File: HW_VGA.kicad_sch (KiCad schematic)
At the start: 6 parts, among them U1 74HC163, U2 74HC163, U3 74HC163, U4 25.175 MHz, U5 74HC11, U6 74HC688

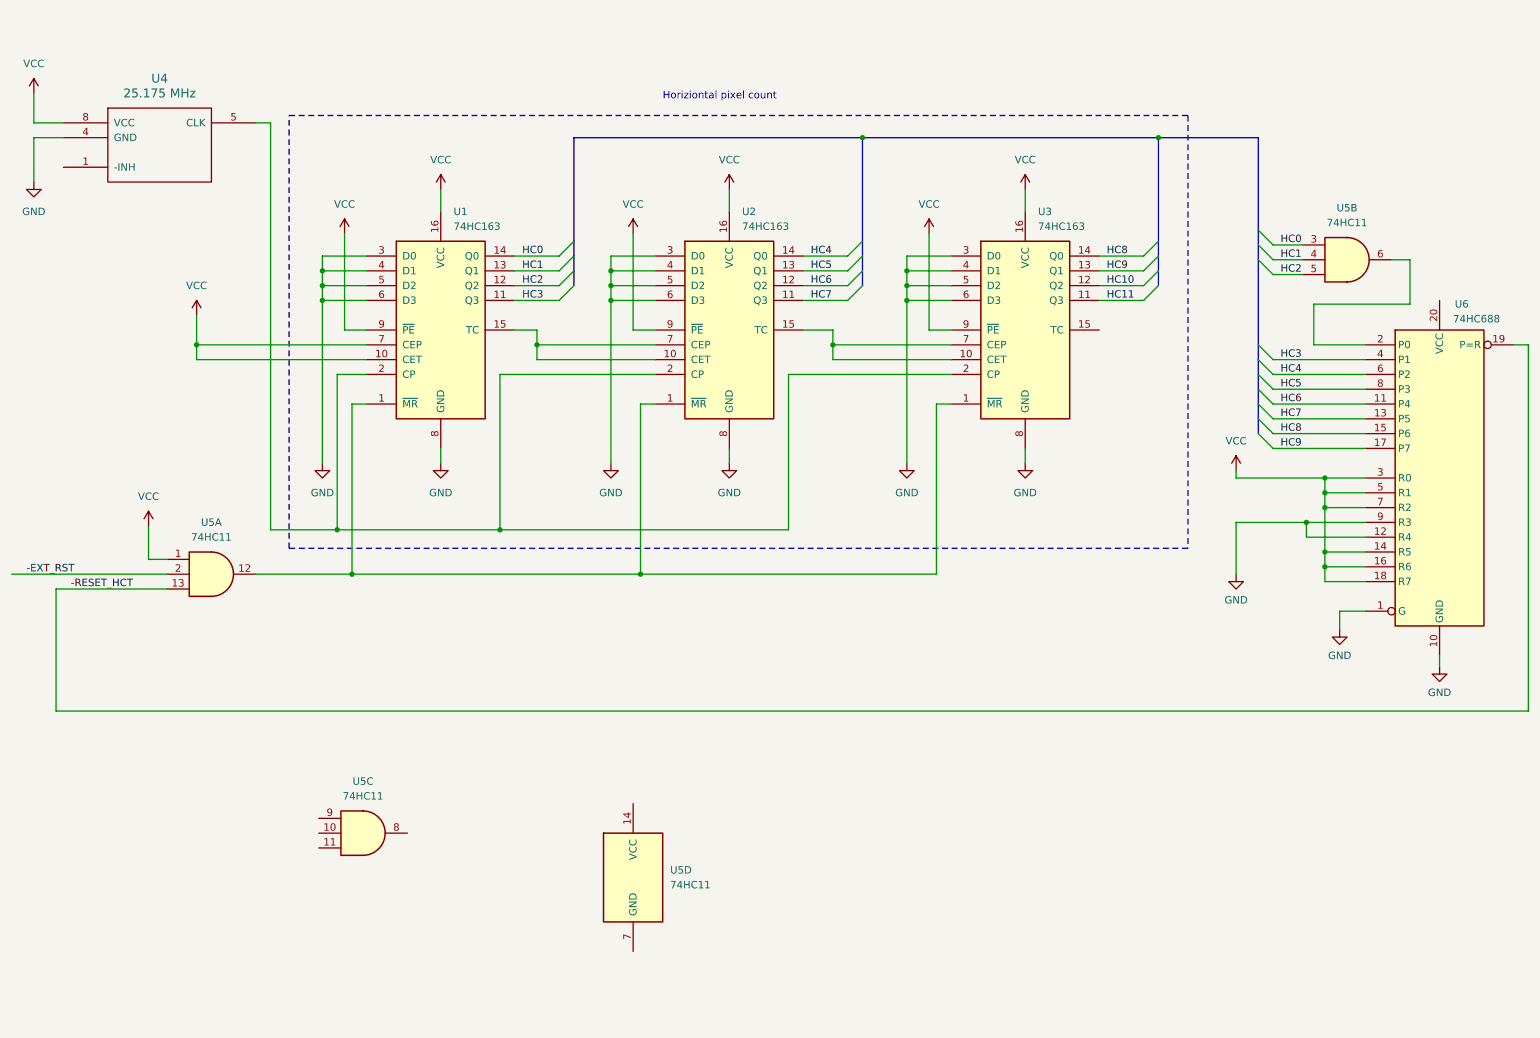
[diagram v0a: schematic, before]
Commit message: move horizontal count module to separate sheet
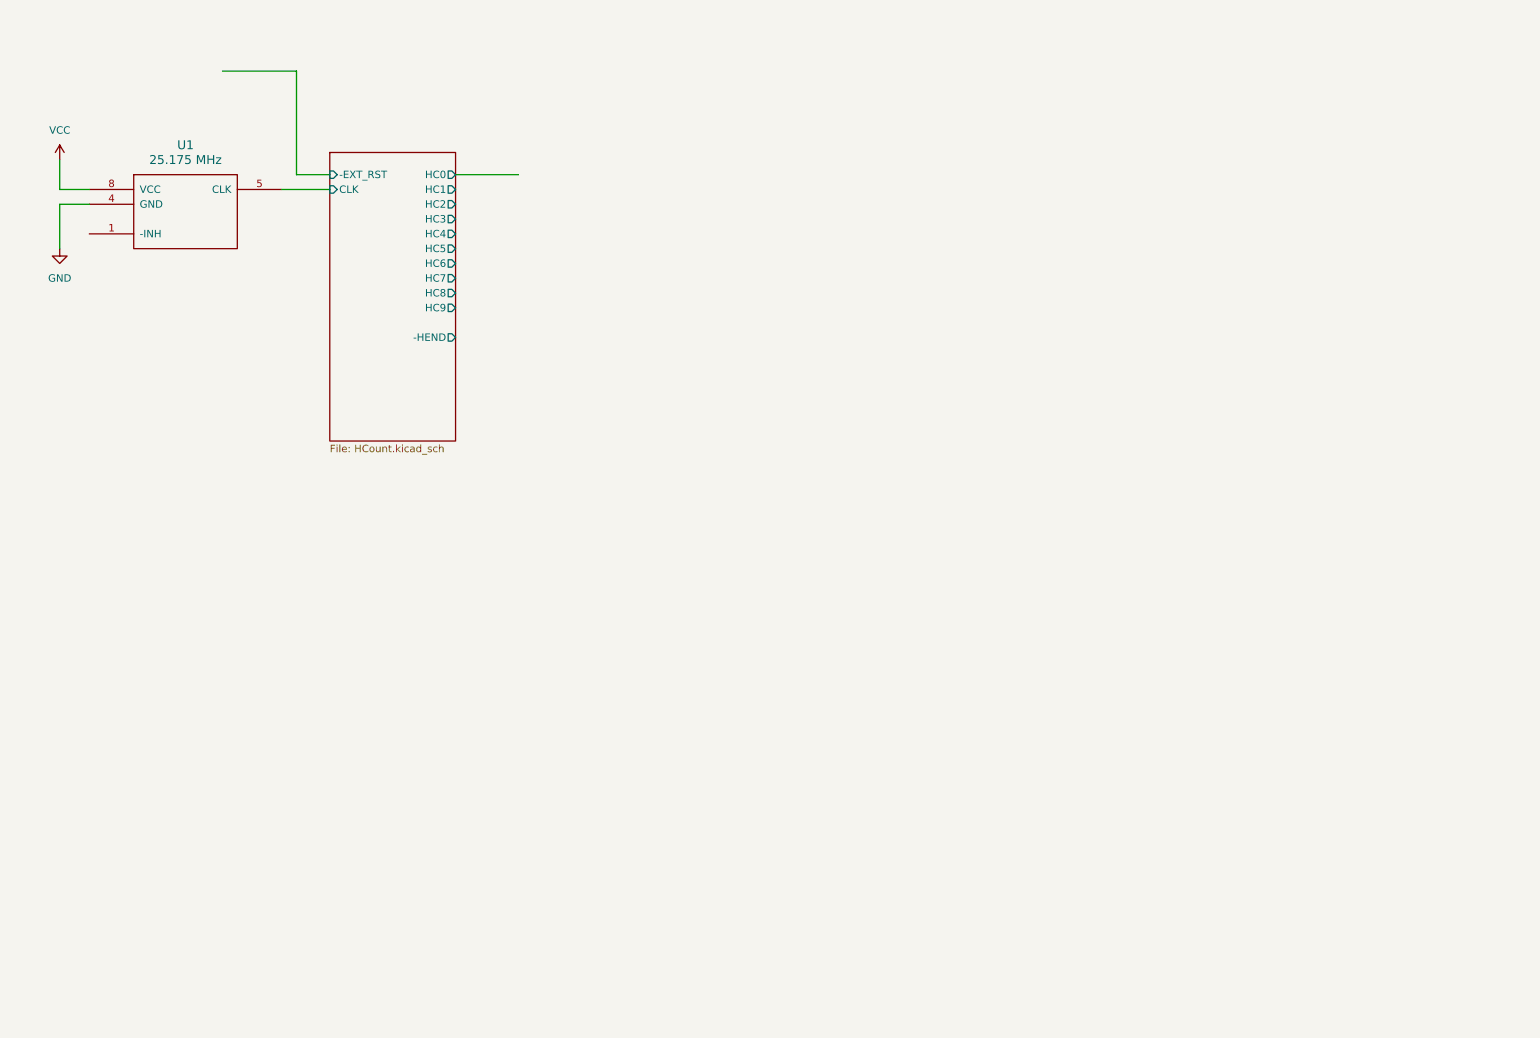
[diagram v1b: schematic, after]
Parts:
- removed U1, U2, U3: 74HC163, symbol 74xx:74LS163
- removed U4: 25.175 MHz, symbol ya68k:XTAL_OSC_HALF_CAN
- removed U5: 74HC11, symbol 74xx:74LS11
- removed U6: 74HC688, symbol 74xx:74LS688
- added U1: 25.175 MHz, symbol ya68k:XTAL_OSC_HALF_CAN
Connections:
- net GND: now also U1.4 (GND)
- net VCC: now also U1.8 (VCC)
- new net HCount/CLK: U1.5 (CLK)
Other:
- added sheet HCount (HCount.kicad_sch)
- note removed: "Horiziontal pixel count"
- company: (none) -> daveho hacks
- title: (none) -> Hardware VGA

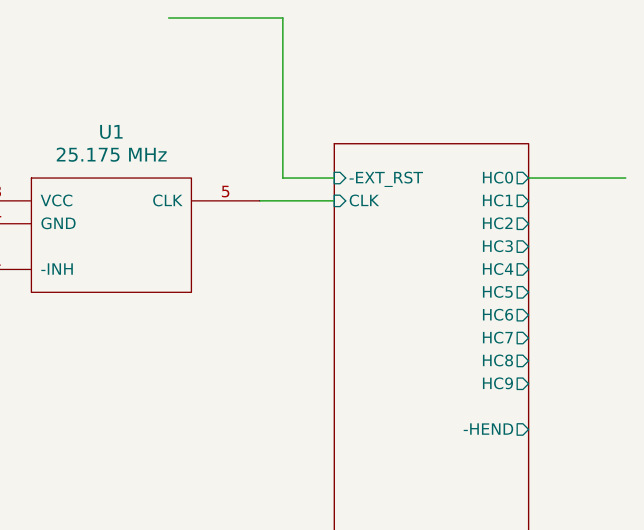
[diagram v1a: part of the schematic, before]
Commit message: allow hcount reset when frame ends
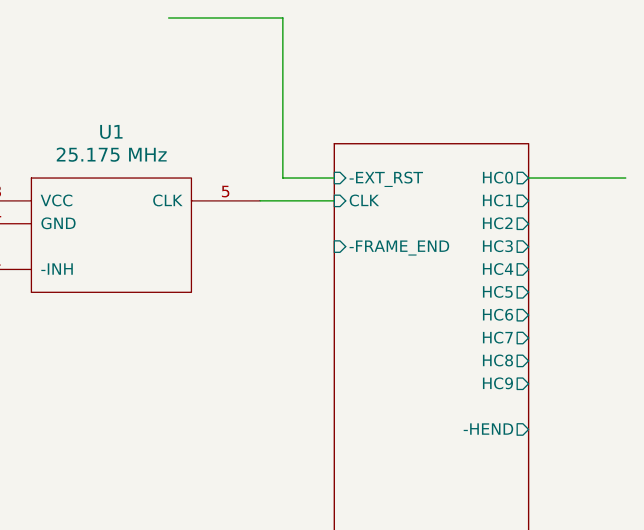
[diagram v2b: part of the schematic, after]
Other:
- sheet HCount ports: added -FRAME_END; removed none
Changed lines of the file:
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@@
       (effects (font (size 1.27 1.27)) (justify right))
+    )
+    (pin "-FRAME_END" input (at 73.66 50.8 180)
+      (effects (font (size 1.27 1.27)) (justify left))
     )
     (instances

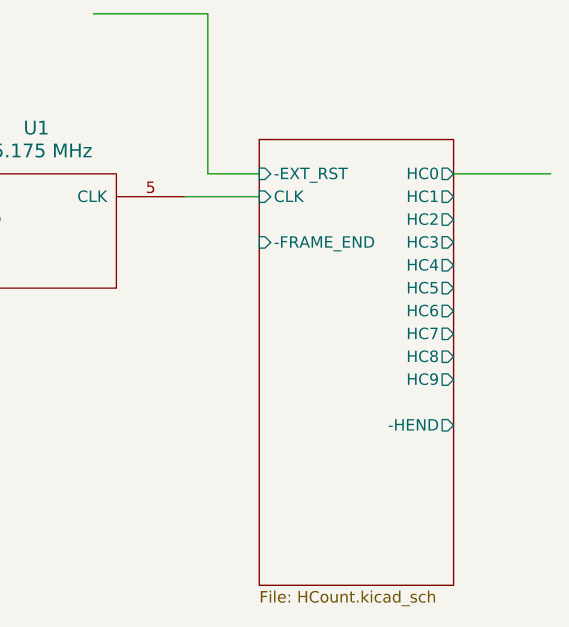
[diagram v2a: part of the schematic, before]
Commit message: replace horizontal count logic with GAL22V10
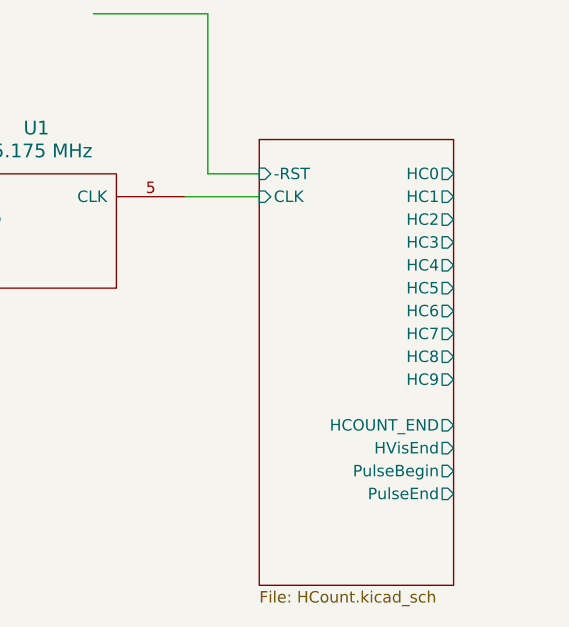
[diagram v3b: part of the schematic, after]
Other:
- sheet HCount ports: added -RST, HCOUNT_END, HVisEnd, PulseBegin, PulseEnd; removed -EXT_RST, -FRAME_END, -HEND

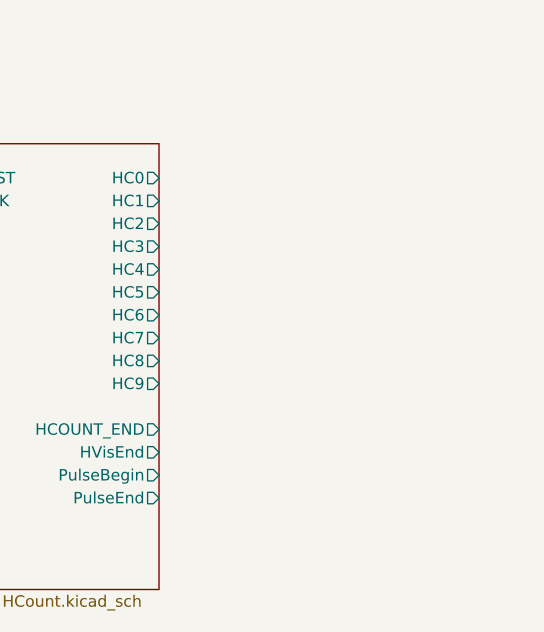
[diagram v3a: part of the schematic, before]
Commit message: start working on VCount module
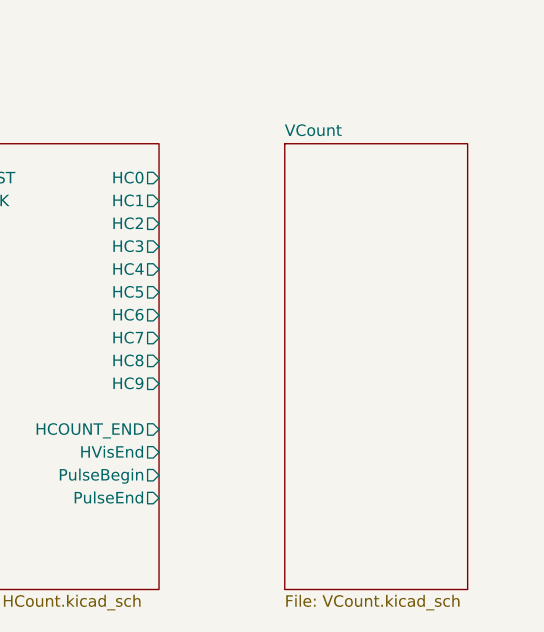
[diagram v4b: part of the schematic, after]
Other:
- added sheet VCount (VCount.kicad_sch)
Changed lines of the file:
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@@
+		)
+	)
+	(sheet
+		(at 109.22 39.37)
+		(size 20.32 49.53)
+		(fields_autoplaced yes)
+		(stroke
+			(width 0.1524)
+			(type solid)
+		)
+		(fill
+			(color 0 0 0 0.0000)
+		)
+		(property "Sheetname" "VCount"
+			(at 109.22 38.6584 0)
+			(effects
+				(font
+					(size 1.27 1.27)
+				)
+				(justify left bottom)
+			)
+		)
+		(property "Sheetfile" "VCount.kicad_sch"
+			(at 109.22 89.4846 0)
+			(effects
+				(font
+					(size 1.27 1.27)
+				)
+				(justify left top)
+			)
+		)
+		(instances
+			(project "HW_VGA"
+				(path "/c4bd4b39-993a-4195-805f-b4de6fa4aea5"
+					(page "3")
+				)
+			)
 		)
 	)

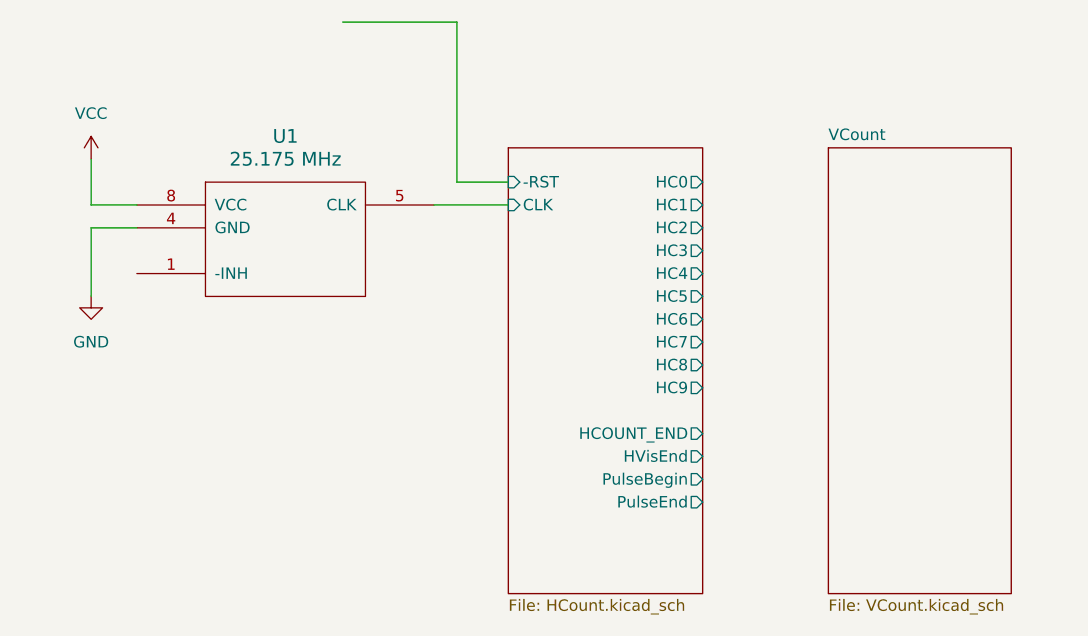
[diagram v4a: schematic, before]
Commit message: set VCOUNT initially in vertical back porch
This means that VVis should *not* be asserted
initially, but should only be asserted once
the first proper frame begins.
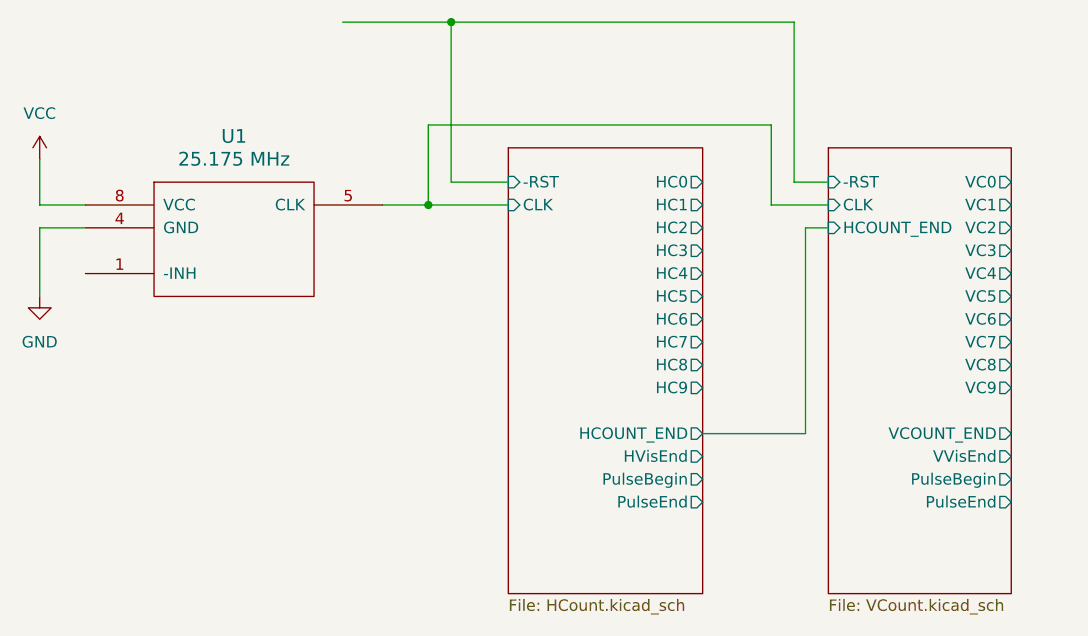
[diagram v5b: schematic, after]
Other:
- sheet VCount ports: added -RST, CLK, HCOUNT_END, PulseBegin, PulseEnd, VC0, VC1, VC2, VC3, VC4, VC5, VC6, VC7, VC8, VC9, VCOUNT_END, VVisEnd; removed none
- moved on the sheet: U1

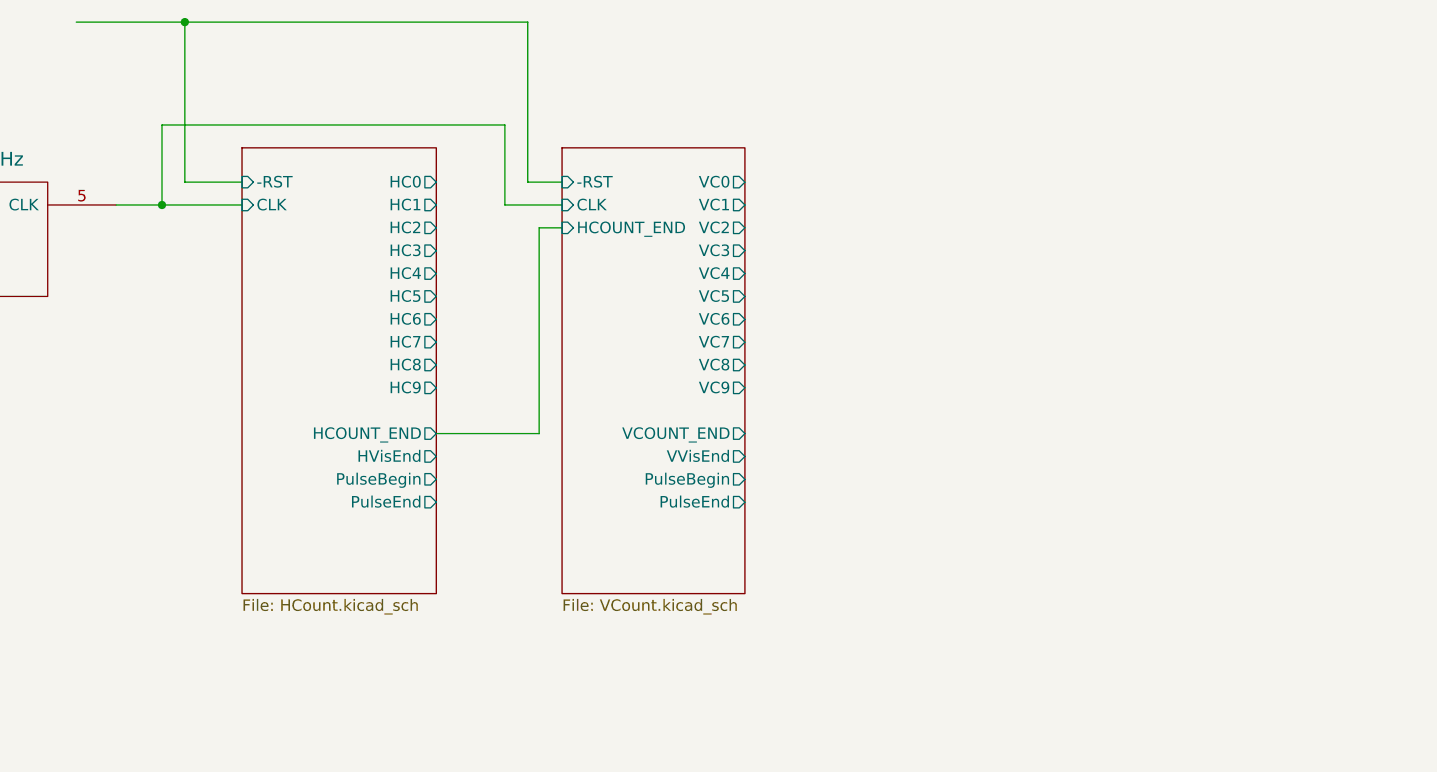
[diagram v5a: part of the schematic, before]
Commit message: add Sync GAL (needs to be 22V10)
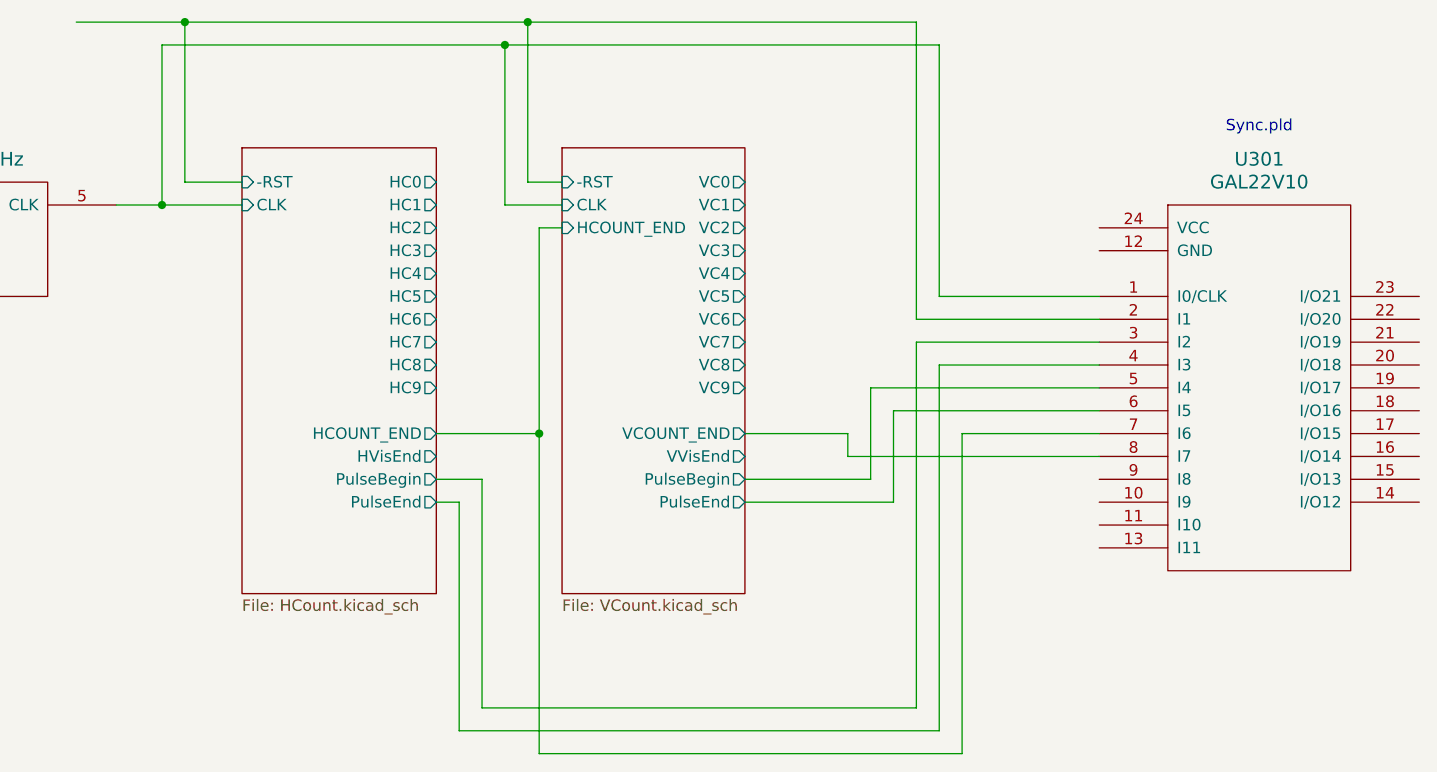
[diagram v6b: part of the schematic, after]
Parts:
- added U301: GAL22V10, symbol ya68k:GAL22V10
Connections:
- net HCount/-RST: now also U301.2 (I1)
- net HCount/CLK: now also U301.1 (I0/CLK)
- net HCount/HCOUNT_END: now also U301.7 (I6)
- net HCount/PulseBegin: now also U301.3 (I2)
- net HCount/PulseEnd: now also U301.4 (I3)
- net VCount/PulseBegin: now also U301.5 (I4)
- net VCount/PulseEnd: now also U301.6 (I5)
- net VCount/VCOUNT_END: now also U301.8 (I7)
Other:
- note added: "Sync.pld"
